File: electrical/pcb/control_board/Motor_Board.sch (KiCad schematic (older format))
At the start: 79 parts, among them J1 ED2627-ND, J11 S7038-ND, J12 PPTC102LFBN-RC, J13 XT60-F, J14 ED2989-ND-USB, J15 XT60-F, J16 XT60-F, J17 Molex_172675-0613, J18 Molex_172675-0613, J19 Molex_172675-0613, J2 ED2627-ND, J20 Molex_172675-0613, J21 Molex_172675-0613, J22 Molex_172675-0613, J28 XT60-F, J29 XT60-F, J3 ED2627-ND, J30 XT60-F, J31 PPTC061LFBN-RC, J33 ina260_Vin, J34 ina260_8pin, J35 PPTC041LFBN-RC, J36 PPTC041LFBN-RC, J37 PPTC041LFBN-RC, J38 PPTC041LFBN-RC, J39 PPTC041LFBN-RC, J40 PPTC041LFBN-RC, J41 PPTC031LFBN-RC, J42 PPTC031LFBN-RC, J43 PPTC031LFBN-RC, J44 PPTC031LFBN-RC, J47 PPTC041LFBN-RC, J48 PPTC041LFBN-RC, J49 PPTC041LFBN-RC, J50 PPTC041LFBN-RC, J51 PPTC041LFBN-RC, J52 PPTC041LFBN-RC, J53 PEC08SAAN, J9 S7038-ND, M1 Mounting_Holes, T1 test_point, T2 test_point, T3 test_point, T4 test_point, T5 test_point, T6 test_point, y1 rover_silkscreen

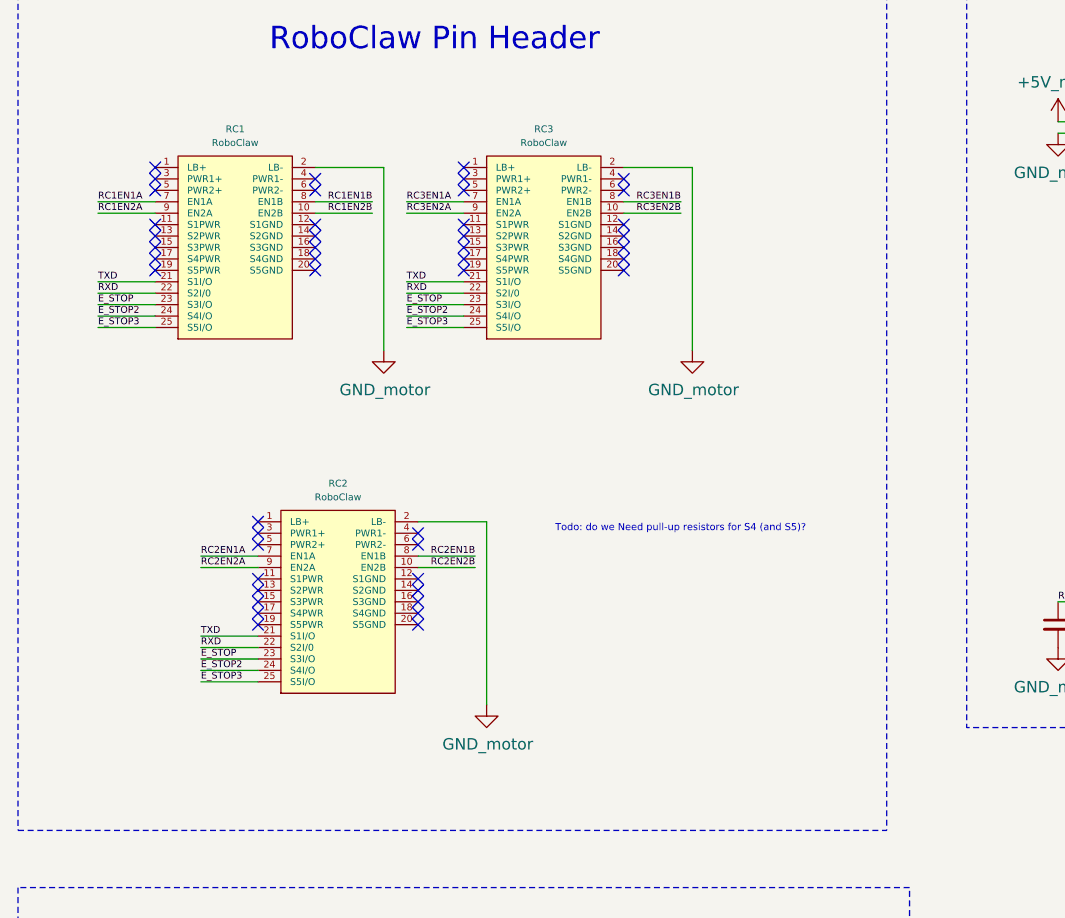
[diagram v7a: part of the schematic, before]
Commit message: add resistors for estops
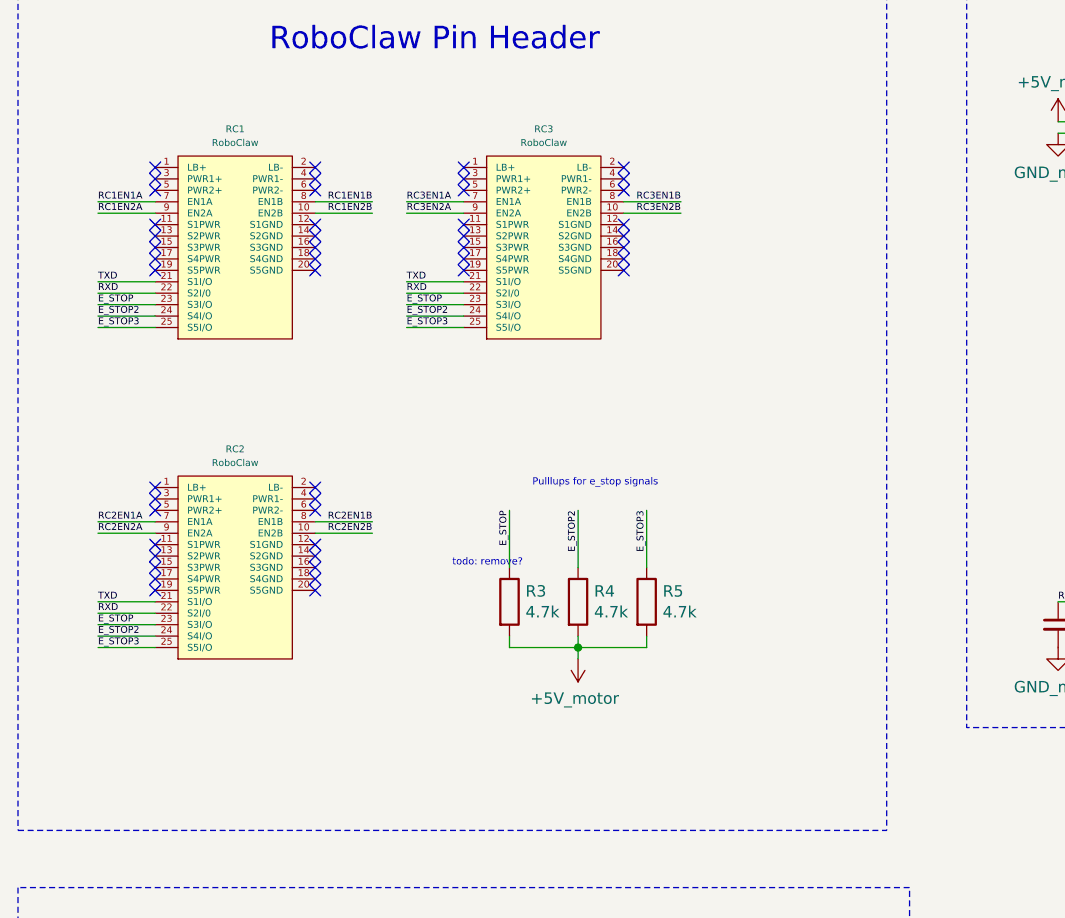
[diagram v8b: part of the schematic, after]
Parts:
- added R3, R4, R5: 4.7k, symbol Device:R
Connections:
- wire segments 265 -> 268
- no-connect marks 92 -> 95
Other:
- note added: "Pulllups for e_stop signals"
- note added: "todo: remove?"
- note removed: "Todo: do we Need pull-up resistors for S4 (and S5)?\n"
- moved on the sheet: RC2
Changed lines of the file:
@@
 	1    0    0    -1
 $EndComp
-Wire Wire Line
-	2600 1750 2600 2550
 Text Label 1350 1900 0    30   ~ 0
 RC1EN1A
@@
 Text Label 2550 1900 2    30   ~ 0
 RC1EN1B
-Wire Wire Line
-	2300 1750 2600 1750
 Wire Wire Line
 	2300 1900 2550 1900
@@
 	1    0    0    -1
 $EndComp
-Wire Wire Line
-	3950 1750 3950 2550
-Text Label 1800 3450 0    30   ~ 0
+Text Label 1350 3300 0    30   ~ 0
 RC2EN1A
-Text Label 1800 3500 0    30   ~ 0
+Text Label 1350 3350 0    30   ~ 0
 RC2EN2A
-Text Label 3000 3450 2    30   ~ 0
+Text Label 2550 3300 2    30   ~ 0
 RC2EN1B
 Wire Wire Line
-	3650 1750 3950 1750
-Wire Wire Line
-	2750 3450 3000 3450
-Wire Wire Line
-	2750 3500 3000 3500
-Text Label 3000 3500 2    30   ~ 0
+	2300 3300 2550 3300
+Wire Wire Line
+	2300 3350 2550 3350
+Text Label 2550 3350 2    30   ~ 0
 RC2EN2B
 Wire Wire Line
-	1800 3450 2050 3450
-Wire Wire Line
-	1800 3500 2050 3500
+	1350 3300 1600 3300
+Wire Wire Line
+	1350 3350 1600 3350
 Wire Wire Line
 	2950 2250 2700 2250
@@
 	2700 1950 2950 1950
 Wire Wire Line
-	3050 3300 3050 4100
-Wire Wire Line
-	2750 3300 3050 3300
-Wire Wire Line
-	2050 3800 1800 3800
-Wire Wire Line
-	2050 3850 1800 3850
-Text Label 1800 3800 0    30   ~ 0
+	1600 3650 1350 3650
+Wire Wire Line
+	1600 3700 1350 3700
+Text Label 1350 3650 0    30   ~ 0
 TXD
-Text Label 1800 3850 0    30   ~ 0
+Text Label 1350 3700 0    30   ~ 0
 RXD
 Wire Wire Line
-	2050 3900 1800 3900
-Text Label 1800 3900 0    30   ~ 0
+	1600 3750 1350 3750
+Text Label 1350 3750 0    30   ~ 0
 E_STOP
 Wire Wire Line
@@
 NoConn ~ 3650 2150
 NoConn ~ 3650 2200
-NoConn ~ 2050 3350
-NoConn ~ 2050 3400
-NoConn ~ 2050 3550
-NoConn ~ 2050 3600
-NoConn ~ 2050 3650
-NoConn ~ 2050 3700
-NoConn ~ 2050 3750
-NoConn ~ 2750 3350
-NoConn ~ 2750 3400
-NoConn ~ 2750 3550
-NoConn ~ 2750 3600
-NoConn ~ 2750 3650
-NoConn ~ 2750 3700
-NoConn ~ 2750 3750
+NoConn ~ 1600 3200
+NoConn ~ 1600 3250
+NoConn ~ 1600 3400
+NoConn ~ 1600 3450
+NoConn ~ 1600 3500
+NoConn ~ 1600 3550
+NoConn ~ 1600 3600
+NoConn ~ 2300 3200
+NoConn ~ 2300 3250
+NoConn ~ 2300 3400
+NoConn ~ 2300 3450
+NoConn ~ 2300 3500
+NoConn ~ 2300 3550
+NoConn ~ 2300 3600
 Text Label 11000 1700 0    30   ~ 0
 RC1M1A
@@
 $EndComp
 $Comp
-L JPL_Robotics_Lib:GND_motor #PWR0106
-U 1 1 60D5E118
-P 2600 2550
-F 0 "#PWR0106" H 2600 2300 50  0001 C CNN
-F 1 "GND_motor" H 2605 2377 50  0000 C CNN
-F 2 "" H 2600 2550 50  0001 C CNN
-F 3 "" H 2600 2550 50  0001 C CNN
-	1    2600 2550
-	1    0    0    -1
-$EndComp
-$Comp
-L JPL_Robotics_Lib:GND_motor #PWR0107
-U 1 1 60D5EA44
-P 3950 2550
-F 0 "#PWR0107" H 3950 2300 50  0001 C CNN
-F 1 "GND_motor" H 3955 2377 50  0000 C CNN
-F 2 "" H 3950 2550 50  0001 C CNN
-F 3 "" H 3950 2550 50  0001 C CNN
-	1    3950 2550
-	1    0    0    -1
-$EndComp
-$Comp
-L JPL_Robotics_Lib:GND_motor #PWR0109
-U 1 1 60DB2478
-P 3050 4100
-F 0 "#PWR0109" H 3050 3850 50  0001 C CNN
-F 1 "GND_motor" H 3055 3927 50  0000 C CNN
-F 2 "" H 3050 4100 50  0001 C CNN
-F 3 "" H 3050 4100 50  0001 C CNN
-	1    3050 4100
-	1    0    0    -1
-$EndComp
-$Comp
 L JPL_Robotics_Lib:GND_motor #PWR0112
 U 1 1 60FADCD7
@@
 E_STOP2
 Wire Wire Line
-	2050 3950 1800 3950
-Text Label 1800 3950 0    30   ~ 0
+	1600 3800 1350 3800
+Text Label 1350 3800 0    30   ~ 0
 E_STOP2
 Wire Wire Line
@@
 Text Label 7250 8150 1    30   ~ 0
 servo_pwm_ch3
-Text Notes 3350 3350 0    31   ~ 0
-Todo: do we Need pull-up resistors for S4 (and S5)?\n
 NoConn ~ 1600 1750
 NoConn ~ 2950 1750
-NoConn ~ 2050 3300
+NoConn ~ 1600 3150
 Wire Wire Line
 	14600 3250 14950 3250
@@
 L JPL_Robotics_Lib:RoboClaw RC?
 U 1 1 60AB7B1E
-P 2150 4050
+P 1700 3900
 AR Path="/60AB7B1E" Ref="RC?"  Part="1"
 AR Path="/60A51BAC/60AB7B1E" Ref="RC2"  Part="1"
-F 0 "RC2" H 2400 4968 30  0000 C CNN
-F 1 "RoboClaw" H 2400 4908 30  0000 C CNN
-F 2 "JPL Robotics:Roboclaw Mount" H 2400 4950 30  0001 C CNN
-F 3 "" H 2400 4950 30  0001 C CNN
-	1    2150 4050
+F 0 "RC2" H 1950 4818 30  0000 C CNN
+F 1 "RoboClaw" H 1950 4758 30  0000 C CNN
+F 2 "JPL Robotics:Roboclaw Mount" H 1950 4800 30  0001 C CNN
+F 3 "" H 1950 4800 30  0001 C CNN
+	1    1700 3900
 	1    0    0    -1
 $EndComp
@@
 	2950 2450 2700 2450
 Wire Wire Line
-	2050 4000 1800 4000
+	1600 3850 1350 3850
 Text Label 1350 2450 0    30   ~ 0
 E_STOP3
 Text Label 2700 2450 0    30   ~ 0
 E_STOP3
-Text Label 1800 4000 0    30   ~ 0
+Text Label 1350 3850 0    30   ~ 0
 E_STOP3
 Wire Wire Line
@@
 NoConn ~ 14100 3050
 NoConn ~ 14600 3050
+NoConn ~ 2300 3150
+NoConn ~ 2300 1750
+NoConn ~ 3650 1750
+Wire Wire Line
+	3150 3250 3150 3500
+Wire Wire Line
+	3450 3250 3450 3500
+Wire Wire Line
+	3750 3250 3750 3500
+$Comp
+L JPL_Robotics_Lib:+5V_motor #PWR01
+U 1 1 610C772D
+P 3450 3900
+F 0 "#PWR01" H 3450 3750 50  0001 C CNN
+F 1 "+5V_motor" H 3465 4073 50  0000 C CNN
+F 2 "" H 3450 3900 50  0001 C CNN
+F 3 "" H 3450 3900 50  0001 C CNN
+	1    3450 3900
+	-1   0    0    1
+$EndComp
+Text Label 3150 3250 3    30   ~ 0
+E_STOP
+Text Label 3450 3250 3    30   ~ 0
+E_STOP2
+Text Label 3750 3250 3    30   ~ 0
+E_STOP3
+Text Notes 3250 3150 0    31   ~ 0
+Pulllups for e_stop signals
+$Comp
+L Device:R R3
+U 1 1 61145EF5
+P 3150 3650
+F 0 "R3" H 3220 3696 50  0000 L CNN
+F 1 "4.7k" H 3220 3605 50  0000 L CNN
+F 2 "" V 3080 3650 50  0001 C CNN
+F 3 "~" H 3150 3650 50  0001 C CNN
+	1    3150 3650
+	1    0    0    -1
+$EndComp
+$Comp
+L Device:R R4
+U 1 1 6115BE1A
+P 3450 3650
+F 0 "R4" H 3520 3696 50  0000 L CNN
+F 1 "4.7k" H 3520 3605 50  0000 L CNN
+F 2 "" V 3380 3650 50  0001 C CNN
+F 3 "~" H 3450 3650 50  0001 C CNN
+	1    3450 3650
+	1    0    0    -1
+$EndComp
+$Comp
+L Device:R R5
+U 1 1 6115C337
+P 3750 3650
+F 0 "R5" H 3820 3696 50  0000 L CNN
+F 1 "4.7k" H 3820 3605 50  0000 L CNN
+F 2 "" V 3680 3650 50  0001 C CNN
+F 3 "~" H 3750 3650 50  0001 C CNN
+	1    3750 3650
+	1    0    0    -1
+$EndComp
+Wire Wire Line
+	3150 3800 3150 3850
+Wire Wire Line
+	3150 3850 3450 3850
+Wire Wire Line
+	3450 3850 3450 3800
+Wire Wire Line
+	3450 3850 3750 3850
+Wire Wire Line
+	3750 3850 3750 3800
+Connection ~ 3450 3850
+Wire Wire Line
+	3450 3900 3450 3850
+Text Notes 2900 3500 0    31   ~ 0
+todo: remove?
 $EndSCHEMATC
